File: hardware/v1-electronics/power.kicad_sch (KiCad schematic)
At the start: 15 parts

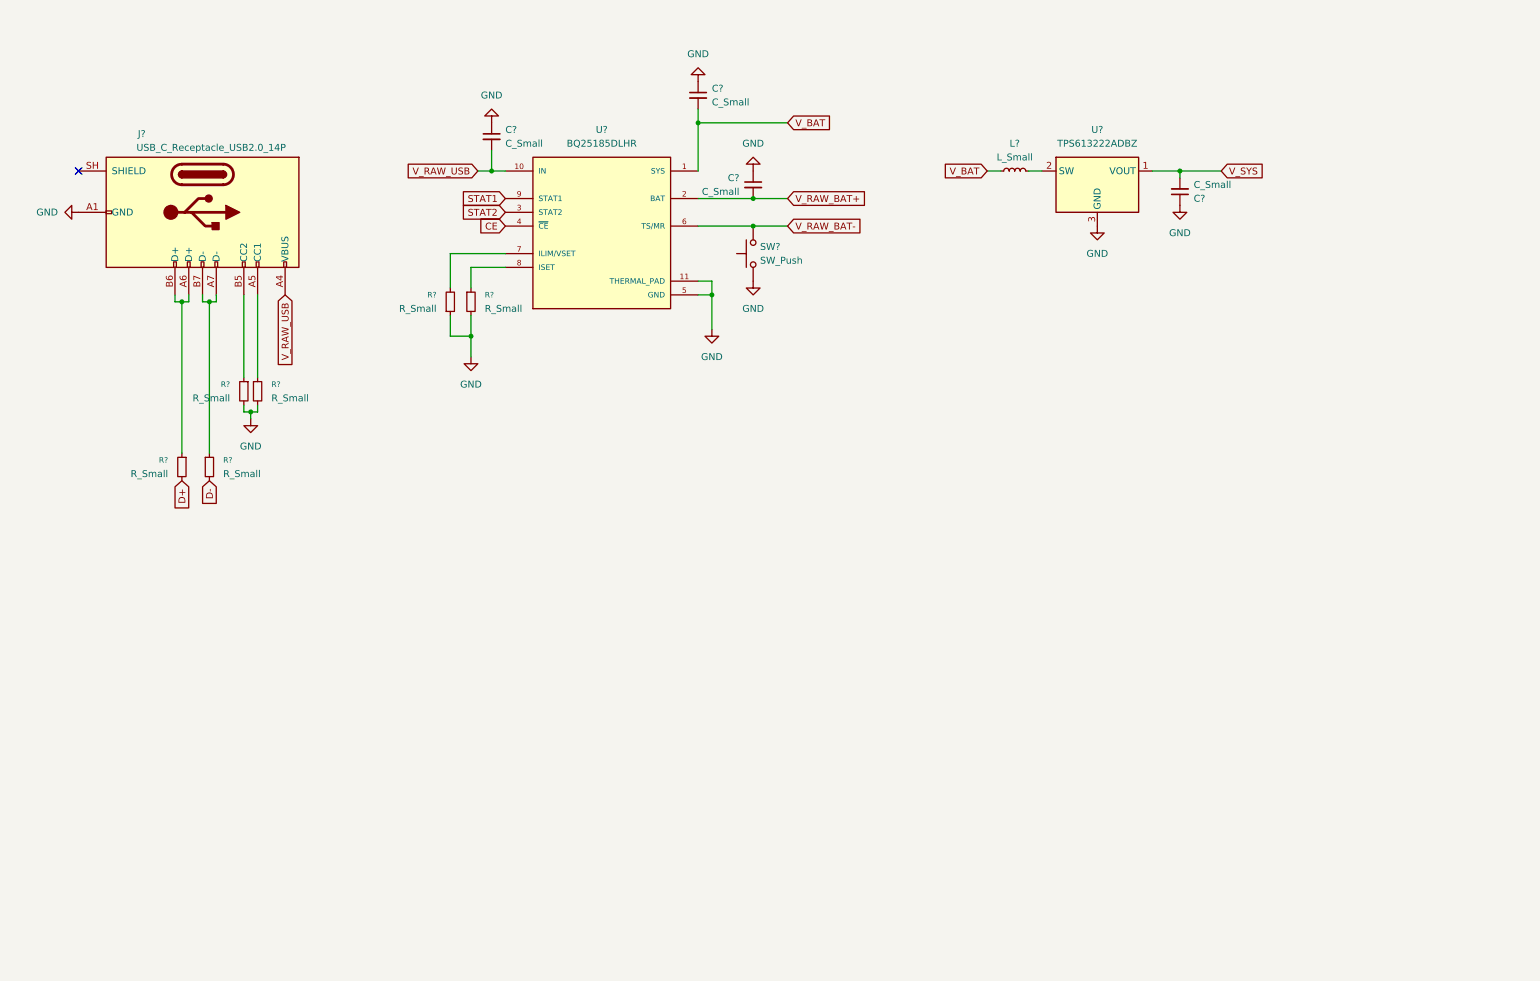
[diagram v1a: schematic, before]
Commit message: refactor(v1 hardware): power train
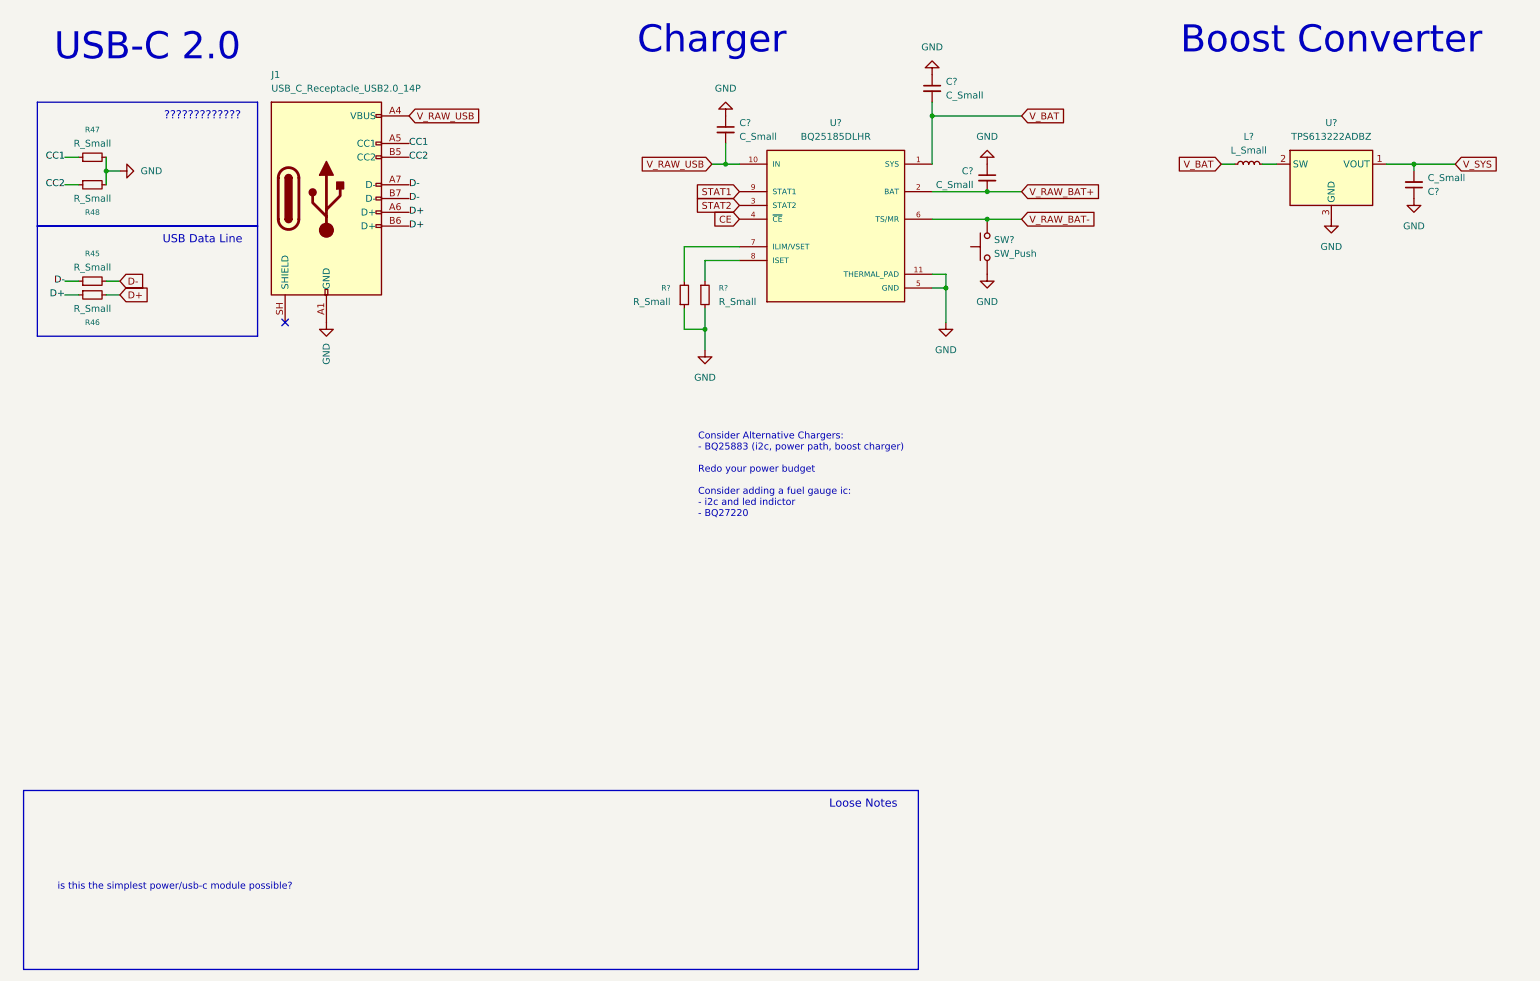
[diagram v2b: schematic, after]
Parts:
- removed J?: USB_C_Receptacle_USB2.0_14P, symbol Connector:USB_C_Receptacle_USB2.0_14P
- removed R? (x4): R_Small, symbol Device:R_Small
- added J1: USB_C_Receptacle_USB2.0_14P, symbol Connector:USB_C_Receptacle_USB2.0_14P
- added R45, R46, R47, R48: R_Small, symbol Device:R_Small
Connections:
- net D+: now also J1.A6 (D+), J1.B6 (D+), R46.1, R46.2
- net D-: now also J1.A7 (D-), J1.B7 (D-), R45.1, R45.2
- net GND: now also J1.A1 (GND), J1.A12 (GND), J1.B1 (GND), J1.B12 (GND), R47.2, R48.2
- net V_RAW_USB: now also J1.A4 (VBUS), J1.A9 (VBUS), J1.B4 (VBUS), J1.B9 (VBUS)
- new net CC1: J1.A5 (CC1), R47.1
- new net CC2: J1.B5 (CC2), R48.1
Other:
- note added: "?????????????"
- note added: "Boost Converter"
- note added: "Charger"
- note added: "Consider Alternative Chargers: - BQ25883 (i2c, power path, boost charger) Redo your power budget Consider adding a fuel gauge ic: - i2c and led indictor - BQ27220"
- note added: "Loose Notes"
- note added: "USB Data Line"
- note added: "USB-C 2.0"
- note added: "is this the simplest power/usb-c module possible?"
- moved on the sheet: C?, L?, R?, SW?, U?

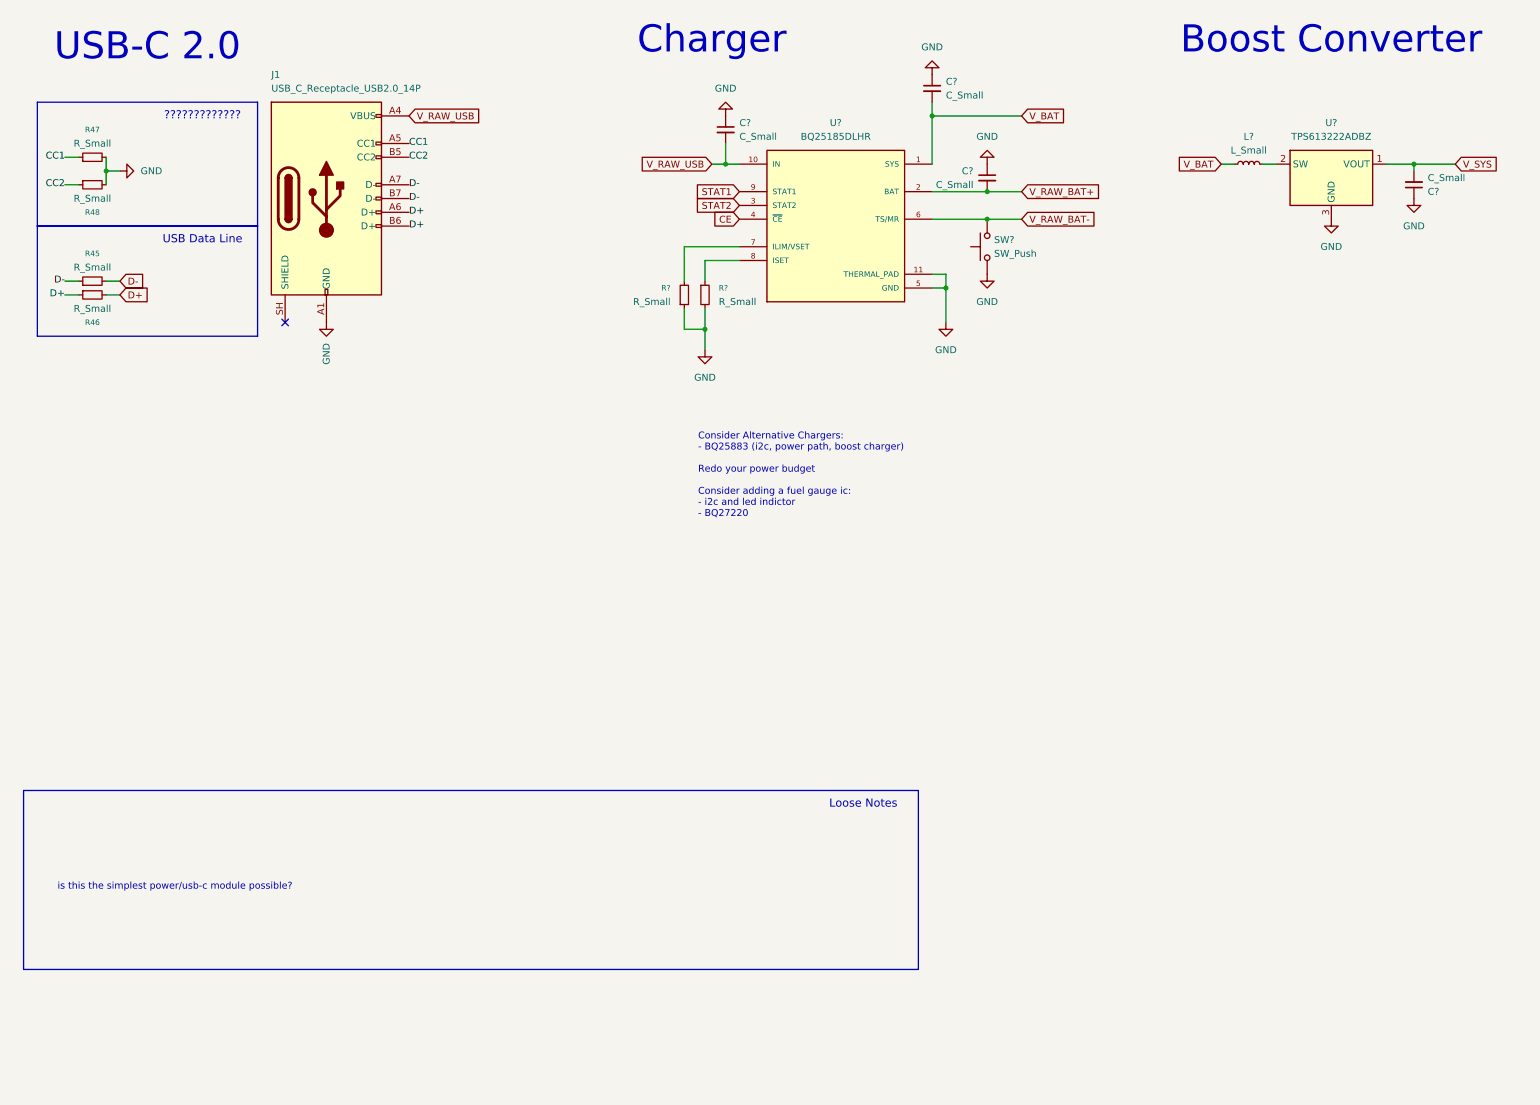
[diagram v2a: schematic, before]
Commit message: refactor(v1 hardware): add different charger ic & clean-up schematics
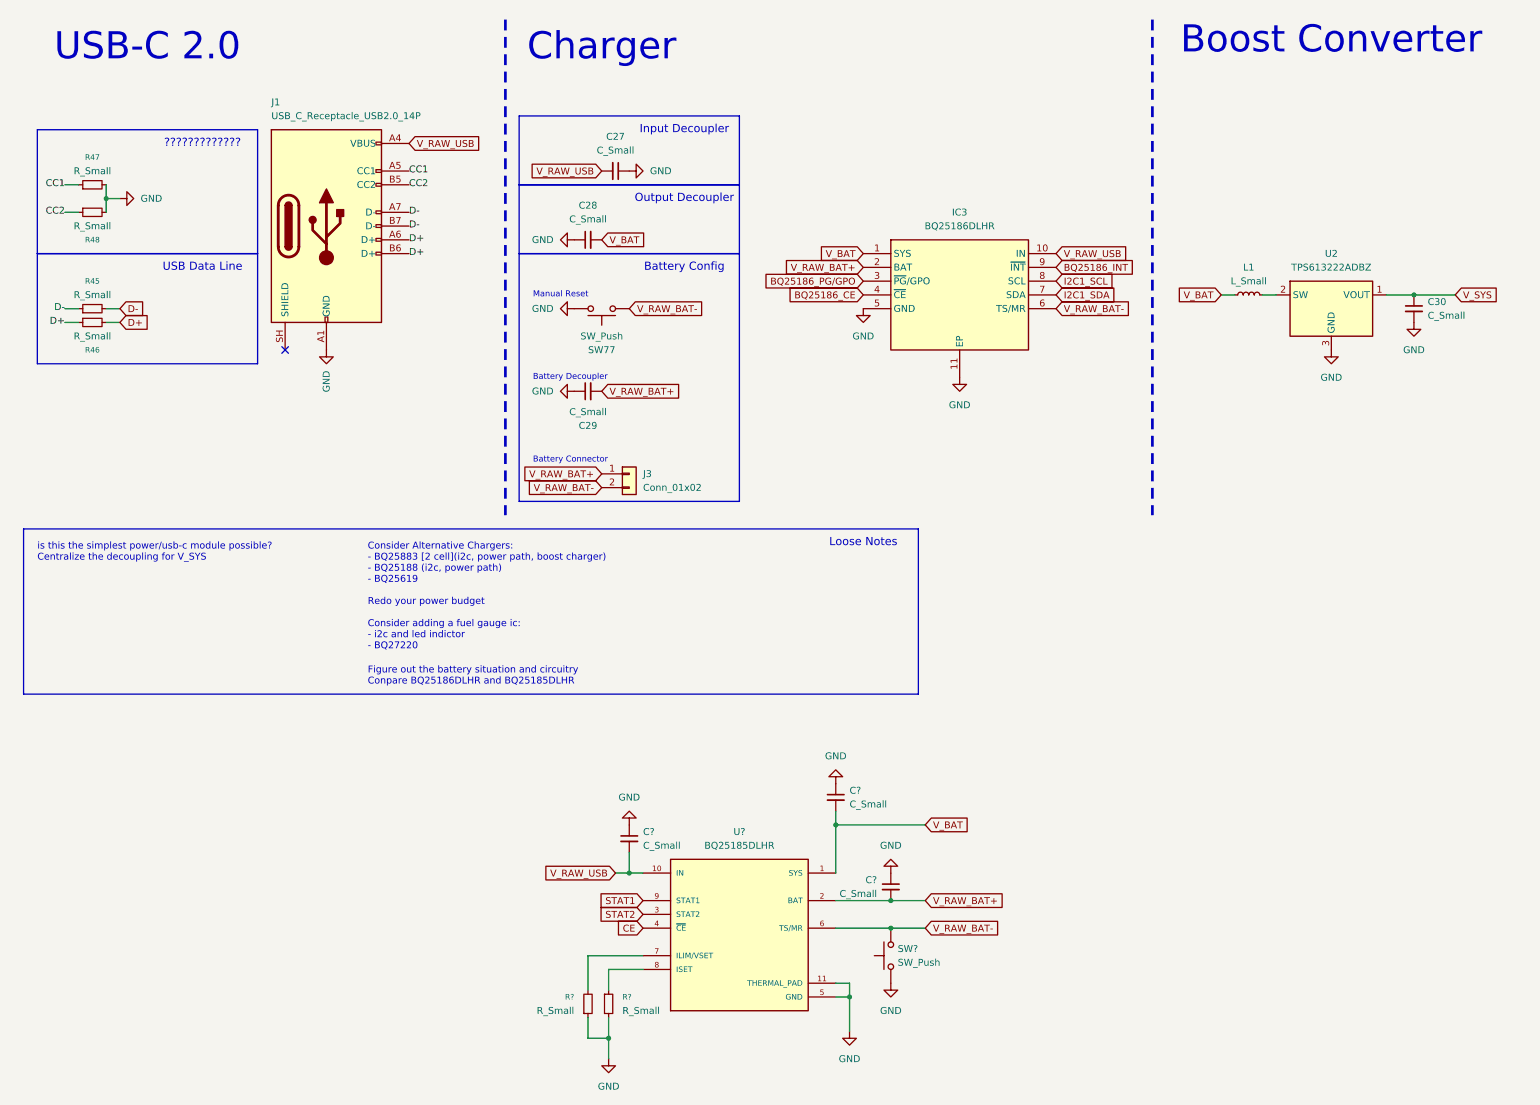
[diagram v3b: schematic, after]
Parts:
- removed C?: C_Small, symbol Device:C_Small
- removed L?: L_Small, symbol Device:L_Small
- removed U?: TPS613222ADBZ, Package_TO_SOT_SMD:SOT-23, symbol Regulator_Switching:TPS613222ADBZ
- added C27, C28, C29, C30: C_Small, symbol Device:C_Small
- added IC3: BQ25186DLHR, Texas Instruments:SON40P220X200X80-11N, symbol Texas Instruments:BQ25186DLHR
- added J3: Conn_01x02, symbol Connector_Generic:Conn_01x02
- added L1: L_Small, symbol Device:L_Small
- added SW77: SW_Push, symbol Switch:SW_Push
- added U2: TPS613222ADBZ, Package_TO_SOT_SMD:SOT-23, symbol Regulator_Switching:TPS613222ADBZ
- U?: footprint BQ25185DLHR:IC_BQ25185DLHR -> Texas Instruments:IC_BQ25185DLHR
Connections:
- net GND: now also C27.1, C28.1, C29.1, C30.2, IC3.11 (EP), IC3.5 (GND), SW77.1, U2.3 (GND)
- net V_BAT: now also C28.2, IC3.1 (SYS), L1.1
- net V_RAW_BAT+: now also C29.2, IC3.2 (BAT), J3.1 (Pin_1)
- net V_RAW_BAT-: now also IC3.6 (TS/MR), J3.2 (Pin_2), SW77.2
- net V_RAW_USB: now also C27.2, IC3.10 (IN)
- net V_SYS: now also C30.1, U2.1 (VOUT)
- new net: L1.2, U2.2 (SW)
- new net BQ25186_CE: IC3.4 (~{CE})
- new net BQ25186_INT: IC3.9 (~{INT})
- new net BQ25186_PG/GPO: IC3.3 (~{PG}/GPO)
- new net I2C1_SCL: IC3.8 (SCL)
- new net I2C1_SDA: IC3.7 (SDA)
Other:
- note added: "Battery Config"
- note added: "Battery Connector"
- note added: "Battery Decoupler"
- note added: "Consider Alternative Chargers: - BQ25883 [2 cell](i2c, power path, boost charger) - BQ25188 (i2c, power path) - BQ25619 Redo your power budget Consider adding a fuel gauge ic: - i2c and led indictor - BQ27220"
- note added: "Figure out the battery situation and circuitry Conpare BQ25186DLHR and BQ25185DLHR"
- note added: "Input Decoupler"
- note added: "Manual Reset"
- note added: "Output Decoupler"
- note added: "is this the simplest power/usb-c module possible? Centralize the decoupling for V_SYS"
- note removed: "Consider Alternative Chargers: - BQ25883 (i2c, power path, boost charger) Redo your power budget Consider adding a fuel gauge ic: - i2c and led indictor - BQ27220"
- note removed: "is this the simplest power/usb-c module possible?"
- moved on the sheet: C?, J1, R45, R46, R47, R48, R?, SW?, U?

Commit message: fix(v1 hardware): fixed the matrix circuit
the change in LED Matrix Driver results in a need to change how we
wire the matrix. this diff accounts for that.

i needed to use a script to rename labels.
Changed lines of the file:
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@@
 	(text "Figure out the battery situation and circuitry\nConpare BQ25186DLHR and BQ25185DLHR"
 		(exclude_from_sim no)
-		(at 76.2 132.08 0)
+		(at 15.24 116.84 0)
 		(effects
 			(font
@@
 		)
 		(stroke
-			(width 0.5)
+			(width 1)
 			(type dash_dot_dot)
 		)
@@
 		)
 		(stroke
-			(width 0.5)
+			(width 1)
 			(type dash_dot_dot)
 		)

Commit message: refactor(v1 hardware): power system
Beefed up power system.
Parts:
- removed C? (x3): C_Small, symbol Device:C_Small
- removed R? (x2): R_Small, symbol Device:R_Small
- removed SW?: SW_Push, symbol Switch:SW_Push
- removed U?: BQ25185DLHR, Texas Instruments:IC_BQ25185DLHR, symbol TI BQ25185DLHR:BQ25185DLHR
- added C31, C32, C34, C47, C48, C49, C50, C51, C52, C53, C54: C_Small, symbol Device:C_Small
- added D86, D87: LED_Small_Filled, symbol Device:LED_Small_Filled
- added IC4: TPS61288LRQQR, PTPS61288RQQR, symbol Texas Instruments:TPS61288LRQQR
- added IC5: MP2721GRH-0000-Z, symbol Monolithic Power Systems:MP2721GRH-0000-Z
- added J4: Conn_01x02, symbol Connector_Generic:Conn_01x02
- added L2: L_Small, symbol Device:L_Small
- added L3: L_Ferrite_Small, symbol Device:L_Ferrite_Small
- added R49, R50, R51, R52, R53, R54: R_Small, symbol Device:R_Small
- added SW78: SW_Push, symbol Switch:SW_Push
- added TH1: Thermistor, symbol Device:Thermistor
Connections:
- net D+: now also IC5.21 (D+)
- net D-: now also IC5.20 (D-)
- net GND: now also C31.2, C34.2, C47.2, C48.2, C50.1, C51.1, C52.1, C54.2, IC4.10 (AGND), IC4.3 (PGND), IC5.18 (AGND), IC5.5 (PGND), J4.2 (Pin_2), R52.2, R54.2, SW78.1, TH1.2
- net I2C1_SCL: now also IC5.16 (SCL)
- net I2C1_SDA: now also IC5.15 (SDA)
- net V_RAW_USB: now also IC5.2 (IN)
- net V_SYS: now also C52.2, IC4.5 (VOUT), R53.1
- new net: D86.2 (A), R49.1
- new net: C31.1, IC5.19 (VCC), R49.2, R50.2
- new net: IC5.10 (NTC1), R51.2, TH1.1
- new net: C32.2, IC5.4 (SW), L2.1
- new net: C34.1, C50.2, IC4.7 (VIN), IC5.13 (SYS), L2.2, L3.1
- new net: C32.1, IC5.6 (BST)
- new net: D87.1 (K), IC5.9 (PG/NTC2)
- new net: D87.2 (A), R50.1
- new net: C53.2, R54.1
- new net: D86.1 (K), IC5.11 (STAT/IB)
- new net: C53.1, C54.1, IC4.2 (COMP)
- new net: C47.1, IC5.3 (PMID)
- new net: IC4.1 (FB), R52.1, R53.2
- new net: C48.1, IC5.12 (BATTSNS), IC5.14 (BATT), J4.1 (Pin_1)
- new net: C49.1, IC4.8 (BST)
- new net: C49.2, IC4.4 (SW_1), L3.2
- new net: C51.2, IC4.11 (VCC)
- new net: IC5.17 (~{RST}), SW78.2
- new net: IC5.7 (VRNTC), R51.1
- new net TPS61288_EN: IC4.6 (EN)
- new net ~{MP2721_INT}: IC5.8 (~{INT})
- no-connect marks 1 -> 2
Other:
- moved on the sheet: C29, IC3, J3, SW77
